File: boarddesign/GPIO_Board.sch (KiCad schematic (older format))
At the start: 63 parts, among them P1 ANA1, P10 I2C_PORT, P11 SPI_PORT, P12 ARM_PORT, P13 RASPBERRY PI GPIO CONN, P14 PROP PLUG, P15 RASPBERRY PI 40-PIN CONN, P16 DIO_PORTA_P1, P17 DIO_PORTA_P2, P18 DIO_PORTA_P3, P19 DIO_PORTA_P4, P2 ANA2, P20 DIO_PORTA_P5, P21 DIO_PORTA_P6, P22 DIO_PORTA_P7, P23 DIO_PORTA_P8, P24 USER COMM, P26 DIO_PORTB_P1, P27 DIO_PORTB_P2, P28 DIO_PORTB_P3, P29 DIO_PORTB_P4, P3 ANA3, P30 DIO_PORTB_P5, P31 DIO_PORTB_P6, P32 DIO_PORTB_P7, P33 DIO_PORTB_P8, P4 ANA4, P5 ANA5, P6 ANA6, P7 ANA7, P8 ANA8, P9 POWER_CONN, Q1 BSS138, U1 MCP3208, U2 P8X32A-D40, U3 24LC256, Y1 5 MHz

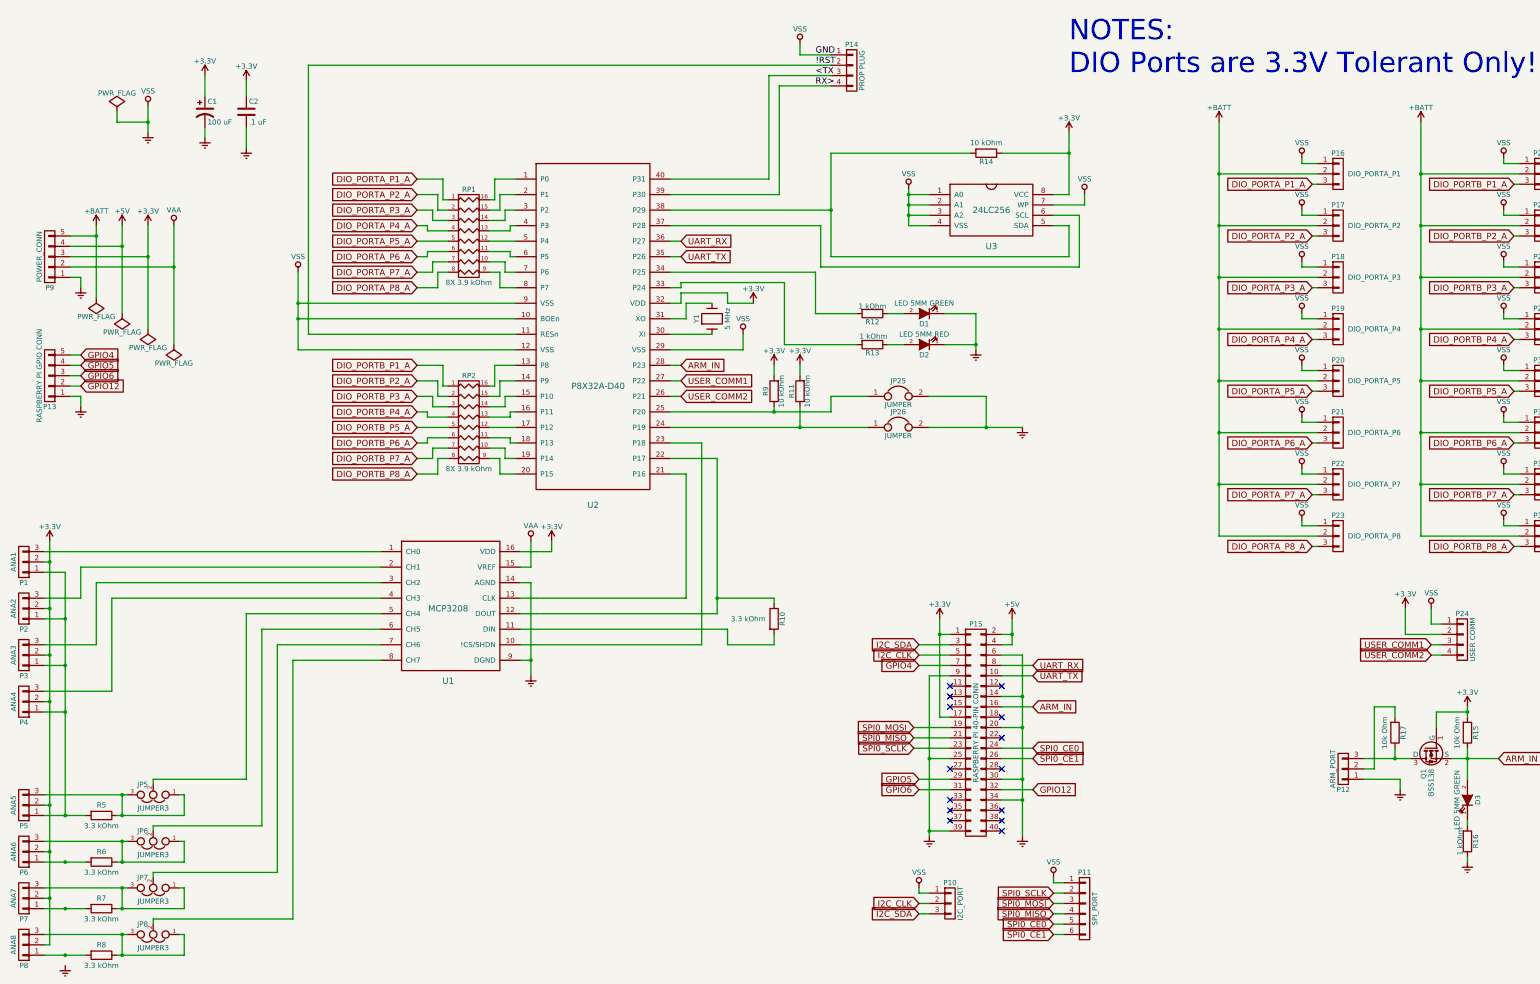
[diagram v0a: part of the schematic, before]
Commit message: Started routing board.
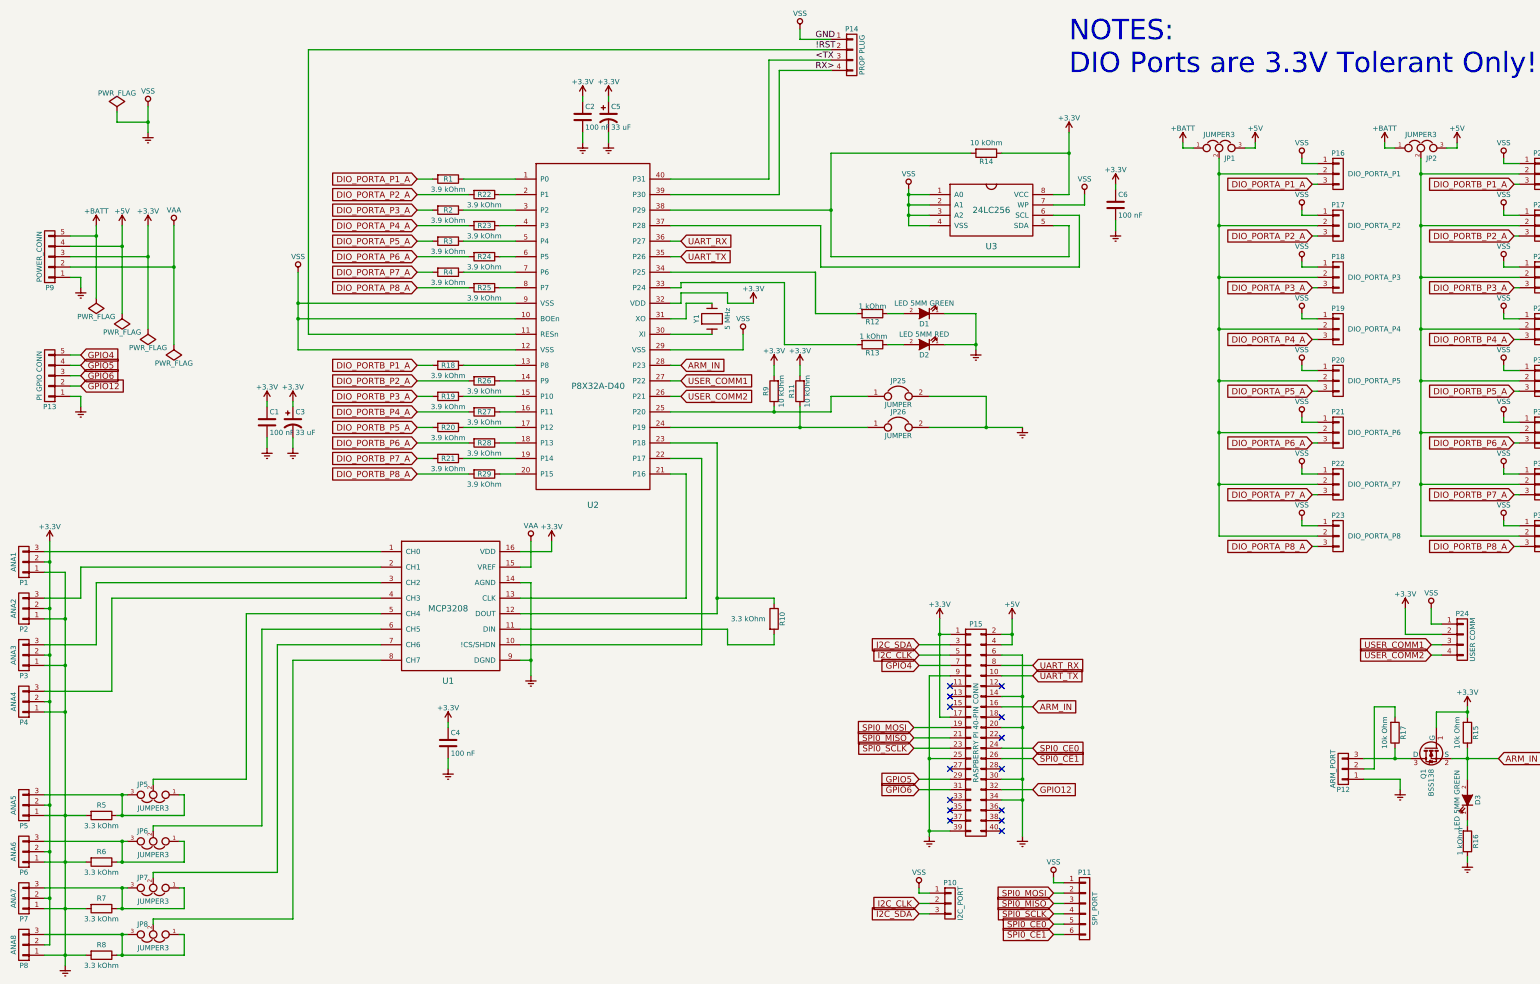
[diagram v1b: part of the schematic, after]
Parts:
- removed C1: 100 uF, Capacitors_ThroughHole:C_Radial_D10_L21_P5, symbol CP1
- removed RP1, RP2: 8X 3.9 kOhm, Housings_DIP:DIP-16_W7.62mm, symbol R_PACK8
- added C1, C4, C6: 100 nF, Capacitors_ThroughHole:C_Rect_L7_W2.5_P5, symbol C
- added C3, C5: 33 uF, Capacitors_ThroughHole:C_Radial_D5_L6_P2.5, symbol CP1
- added JP1, JP2: JUMPER3, Pin_Headers:Pin_Header_Straight_1x03, symbol JUMPER3
- added R1, R18, R19, R2, R20, R21, R22, R23, R24, R25, R26, R27, R28, R29, R3, R4: 3.9 kOhm, Pin_Headers:Pin_Header_Straight_1x02, symbol R
- C2: value .1 uF -> 100 nF
- P12: footprint Pin_Headers:Pin_Header_Straight_1x03 -> Terminal_Blocks:TerminalBlock_Pheonix_MPT-2.54mm_3pol
- P13: value RASPBERRY PI GPIO CONN -> PI GPIO CONN; footprint Pin_Headers:Pin_Header_Straight_1x05 -> Terminal_Blocks:TerminalBlock_Pheonix_MPT-2.54mm_5pol
- P24: footprint Pin_Headers:Pin_Header_Straight_1x04 -> Terminal_Blocks:TerminalBlock_Pheonix_MPT-2.54mm_4pol
- P9: footprint Pin_Headers:Pin_Header_Straight_1x05 -> Terminal_Blocks:TerminalBlock_Pheonix_MPT-2.54mm_5pol
- R5, R6, R7, R8: footprint Resistors_ThroughHole:Resistor_Horizontal_RM10mm -> Pin_Headers:Pin_Header_Straight_1x02
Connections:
- net +3V3: now also C1.1, C3.1, C4.1, C5.1, C6.1
- net +5V: now also JP1.3, JP2.3
- net +BATT: now also JP1.1, JP2.1; no longer P16.2 (P2), P17.2 (P2), P18.2 (P2), P19.2 (P2), P20.2 (P2), P21.2 (P2), P22.2 (P2), P23.2 (P2), P26.2 (P2), P27.2 (P2), P28.2 (P2), P29.2 (P2), P30.2 (P2), P31.2 (P2), P32.2 (P2), P33.2 (P2)
- net DIO_PORTA_P1_A: now also R1.2
- net DIO_PORTA_P2_A: now also R22.2
- net DIO_PORTA_P3_A: now also R2.2
- net DIO_PORTA_P4_A: now also R23.2
- net DIO_PORTA_P5_A: now also R3.2
- net DIO_PORTA_P6_A: now also R24.2
- net DIO_PORTA_P7_A: now also R4.2
- net DIO_PORTA_P8_A: now also R25.2
- net DIO_PORTB_P1_A: now also R18.2
- net DIO_PORTB_P2_A: now also R26.2
- net DIO_PORTB_P3_A: now also R19.2
- net DIO_PORTB_P4_A: now also R27.2
- net DIO_PORTB_P5_A: now also R20.2
- net DIO_PORTB_P6_A: now also R28.2
- net DIO_PORTB_P7_A: now also R21.2
- net DIO_PORTB_P8_A: now also R29.2
- net GNDREF: now also P1.1 (P1), P2.1 (P1), P3.1 (P1), P4.1 (P1), P5.1 (P1), P6.1 (P1), P7.1 (P1), P8.1 (P1), R5.2, R6.2, R7.2, R8.2, C1.2, C3.2, C4.2, C5.2, C6.2
- net SPI0_MISO: now also P11.3 (P3); no longer P11.4 (P4)
- net SPI0_MOSI: now also P11.2 (P2); no longer P11.3 (P3)
- net SPI0_SCLK: now also P11.4 (P4); no longer P11.2 (P2)
- net at U1.10 (!CS/SHDN): now also U2.22 (P17); no longer U2.23 (P18)
- net at R10.1, U1.12 (DOUT): now also U2.23 (P18); no longer U2.22 (P17)
- net at U2.1 (P0): now also R1.1
- net at U2.13 (P8): now also R18.1
- net at U2.14 (P9): now also R26.1
- net at U2.15 (P10): now also R19.1
- net at U2.16 (P11): now also R27.1
- net at U2.17 (P12): now also R20.1
- net at U2.18 (P13): now also R28.1
- net at U2.19 (P14): now also R21.1
- net at U2.2 (P1): now also R22.1
- net at U2.20 (P15): now also R29.1
- net at U2.3 (P2): now also R2.1
- net at U2.4 (P3): now also R23.1
- net at U2.5 (P4): now also R3.1
- net at U2.6 (P5): now also R24.1
- net at U2.7 (P6): now also R4.1
- net at U2.8 (P7): now also R25.1
- new net: JP2.2, P26.2 (P2), P27.2 (P2), P28.2 (P2), P29.2 (P2), P30.2 (P2), P31.2 (P2), P32.2 (P2), P33.2 (P2)
- new net: JP1.2, P16.2 (P2), P17.2 (P2), P18.2 (P2), P19.2 (P2), P20.2 (P2), P21.2 (P2), P22.2 (P2), P23.2 (P2)
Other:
- moved on the sheet: C2, P14
